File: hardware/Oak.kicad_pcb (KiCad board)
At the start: 2 copper layers, 100 x 40 mm, 71 parts, among them J1 18650 Battery holder, J2 USB_B_Micro, J4 Conn_ARM_JTAG_SWD_10, SW1 SW_SPDT, SW2 SW_Push, U1 AP2112, U2 ATSAMD21, U3 MCP7383, U4 PA1010D, U5 RFM95, U6 Waveshare_1in54_epaper

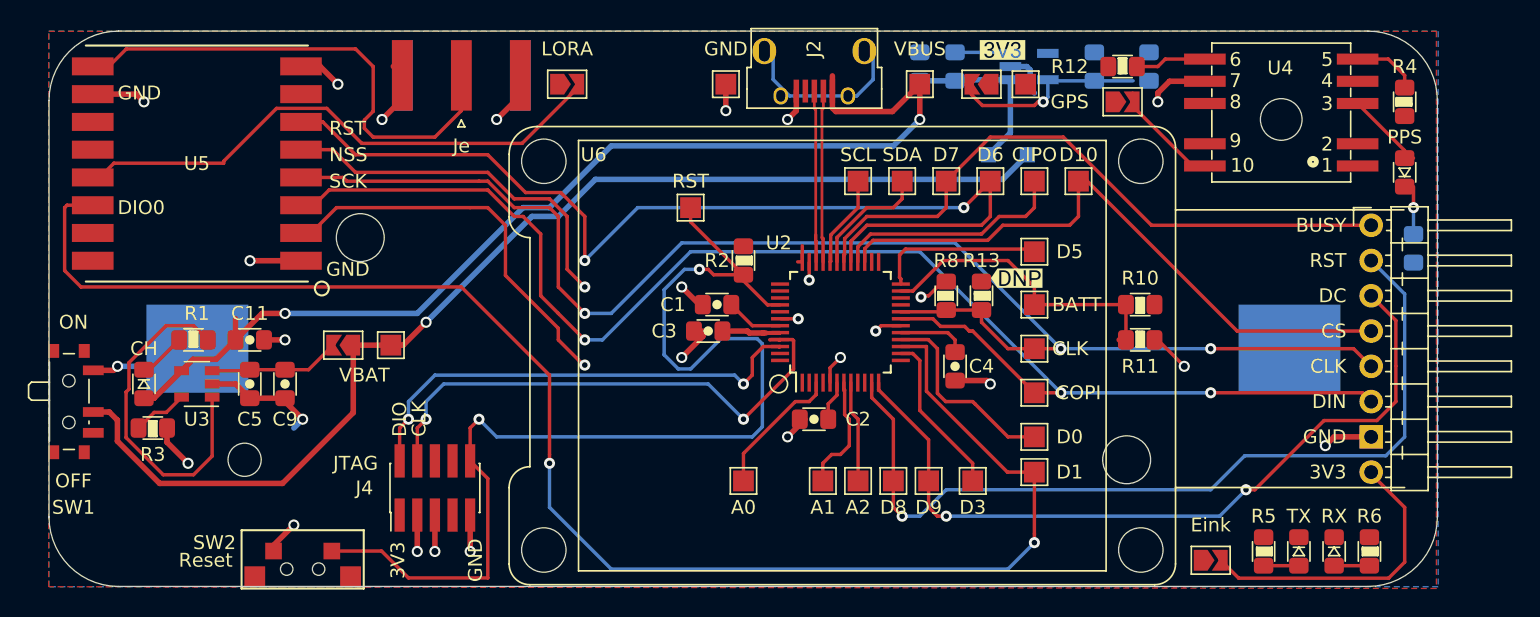
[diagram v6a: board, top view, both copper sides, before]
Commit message: feat: add more routes (0 remaining unconnected)
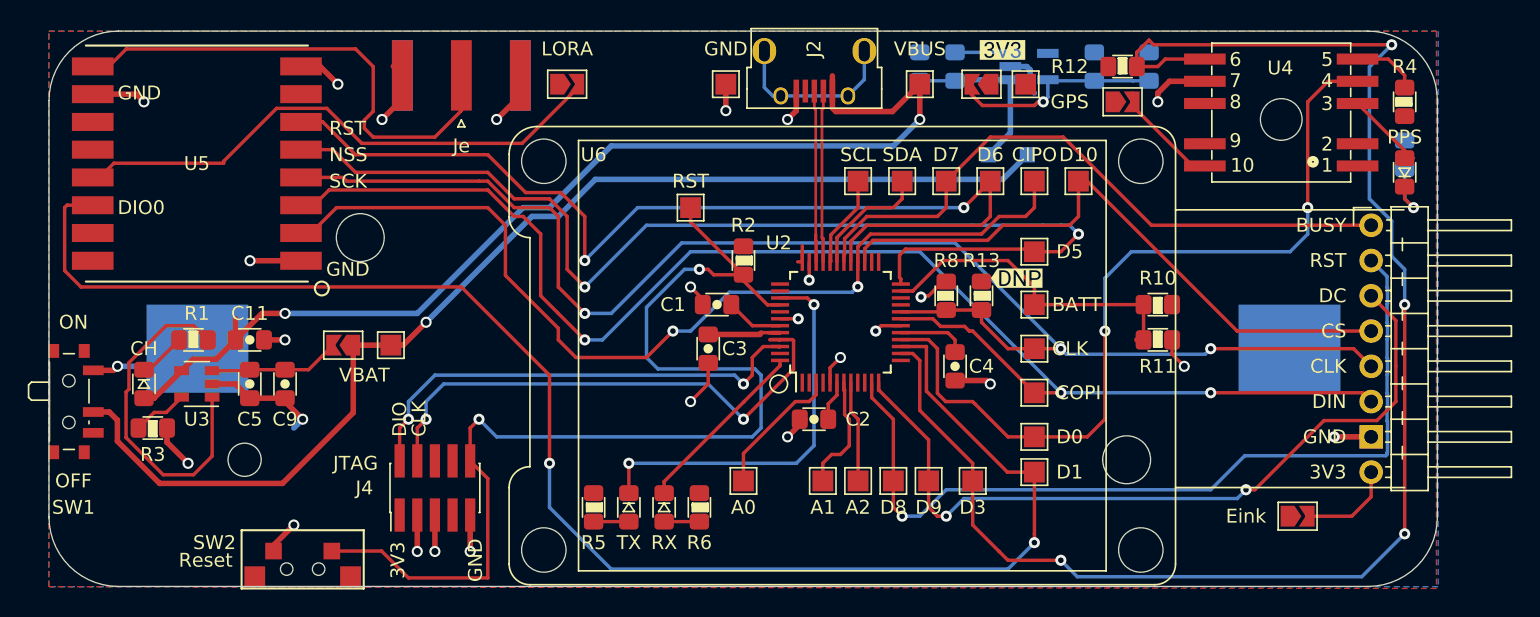
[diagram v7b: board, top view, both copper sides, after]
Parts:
- moved D5 48.4 mm to (137.8, 104.1)
- moved D4 48.4 mm to (135.3, 104.1)
- moved R5 48.4 mm to (132.7, 104.1)
- moved R6 48.4 mm to (140.3, 104.1)
- moved JP5 7.02 mm to (183.4, 104.8)
- moved R7 6.77 mm to (191.1, 78.7), turned to 90 degrees
- moved C3 1.27 mm to (141.0, 92.7), turned to 270 degrees
- moved R10 1.27 mm to (173.4, 89.5)
- moved R11 1.27 mm to (173.4, 92.1)
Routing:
- net /D3: track 17.1 -> 111.0 mm, vias 0 -> 4
- net /D0: track 14.4 -> 59.8 mm, vias 0 -> 2
- net /D5: track 39.4 -> 80.7 mm, vias 1 -> 2
- net /TX_LED: track 0.00 -> 28.8 mm, vias 0 -> 2
- net /CIPO: track 45.9 -> 69.2 mm, vias 1 -> 2
- net Net-(JP5-Pad2): track 21.7 -> 7.06 mm
- net /RX_LED: track 0.00 -> 13.0 mm
- net /VBUS: track 90.4 -> 93.2 mm
- net +3V3: track 14.6 -> 16.1 mm
- net Net-(D3-Pad1): track 3.42 -> 4.83 mm
- net /RST: track 82.5 -> 81.1 mm
- net /BATT: track 22.0 -> 23.2 mm
- net Net-(C6-Pad1): track 14.3 -> 15.4 mm
- net /D8: track 62.8 -> 61.9 mm
- net GND: track 79.7 -> 79.0 mm

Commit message: feat: complete all routes with rendered documents and images
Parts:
- moved svg2mod 0.64 mm to (163.8, 87.6)
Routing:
- net /VBUS: track 93.2 -> 91.7 mm
- net /CLK: track 104.0 -> 102.5 mm
- net /D6: track 73.3 -> 71.8 mm
- net Net-(J3-Pad1): track 36.0 -> 34.8 mm
- net /D5: track 80.7 -> 79.6 mm
